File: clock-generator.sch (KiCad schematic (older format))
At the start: 7 parts

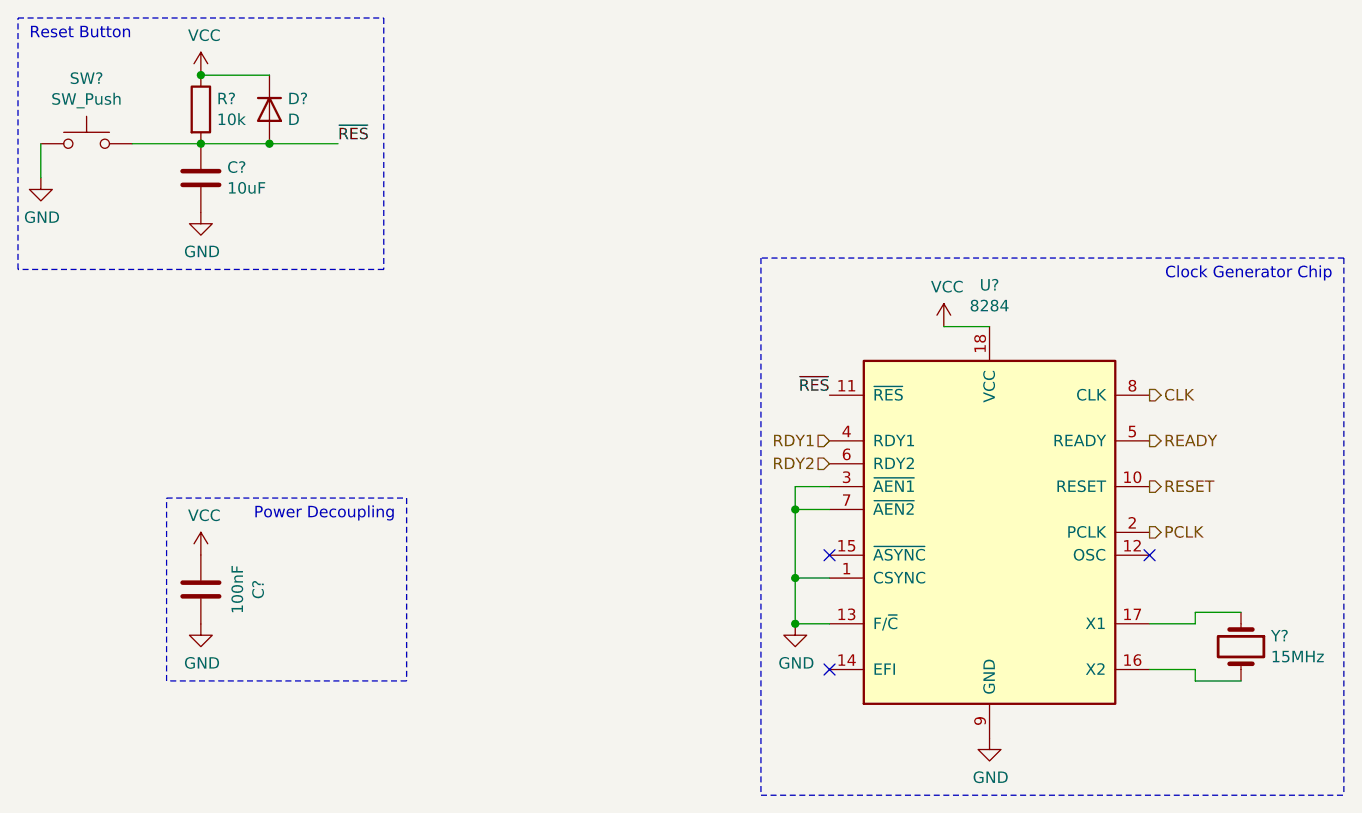
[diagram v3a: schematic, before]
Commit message: General edits; removed floating inputs
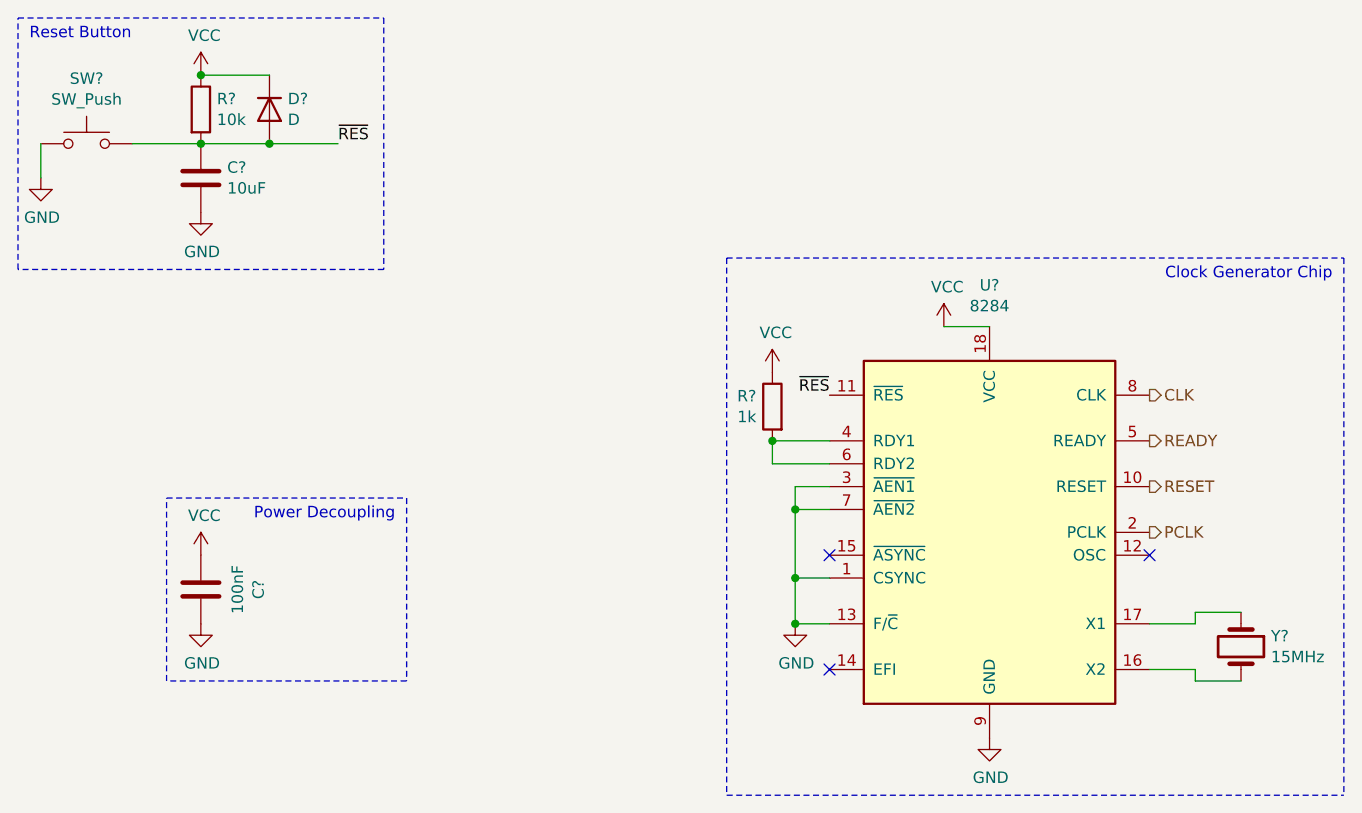
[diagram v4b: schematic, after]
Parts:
- added R?: 1k, symbol Device:R
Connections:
- net RDY2 is gone; now on an unnamed net: U?.6 (RDY2)
- net VCC: now also R?.1
- net RDY1: no longer names the net of U?.4 (RDY1)
- net RDY1: now also R?.2
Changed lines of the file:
@@
 $Descr A4 11693 8268
 encoding utf-8
-Sheet 4 15
+Sheet 3 15
 Title "clock-generator"
 Date ""
@@
 Text HLabel 6400 3200 2    50   Output ~ 0
 READY
-Text HLabel 5000 3200 0    50   Input ~ 0
-RDY1
-Text HLabel 5000 3300 0    50   Input ~ 0
-RDY2
 NoConn ~ 5000 3700
 Wire Wire Line
@@
 $EndComp
 Wire Notes Line
-	7250 2400 4700 2400
-Wire Notes Line
-	4700 2400 4700 4750
-Wire Notes Line
-	4700 4750 7250 4750
-Wire Notes Line
 	7250 2400 7250 4750
 Text Notes 7200 2500 2    50   ~ 0
@@
 Text Notes 1500 1450 0    50   ~ 0
 Reset Button
+Wire Wire Line
+	5000 3300 4750 3300
+Wire Wire Line
+	5000 3200 4750 3200
+Wire Wire Line
+	4750 3300 4750 3200
+$Comp
+L Device:R R?
+U 1 1 61F71673
+P 4750 3050
+F 0 "R?" H 4820 3096 50  0000 L CNN
+F 1 "1k" H 4820 3005 50  0000 L CNN
+F 2 "" V 4680 3050 50  0001 C CNN
+F 3 "~" H 4750 3050 50  0001 C CNN
+	1    4750 3050
+	-1   0    0    -1
+$EndComp
+$Comp
+L power:VCC #PWR?
+U 1 1 61F75C77
+P 4750 2900
+F 0 "#PWR?" H 4750 2750 50  0001 C CNN
+F 1 "VCC" H 4765 3073 50  0000 C CNN
+F 2 "" H 4750 2900 50  0001 C CNN
+F 3 "" H 4750 2900 50  0001 C CNN
+	1    4750 2900
+	1    0    0    -1
+$EndComp
+Connection ~ 4750 3200
+Wire Notes Line
+	4550 2400 4550 4750
+Wire Notes Line
+	4550 2400 7250 2400
+Wire Notes Line
+	4550 4750 7250 4750
 $EndSCHEMATC

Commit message: Assign footprints for most symbols
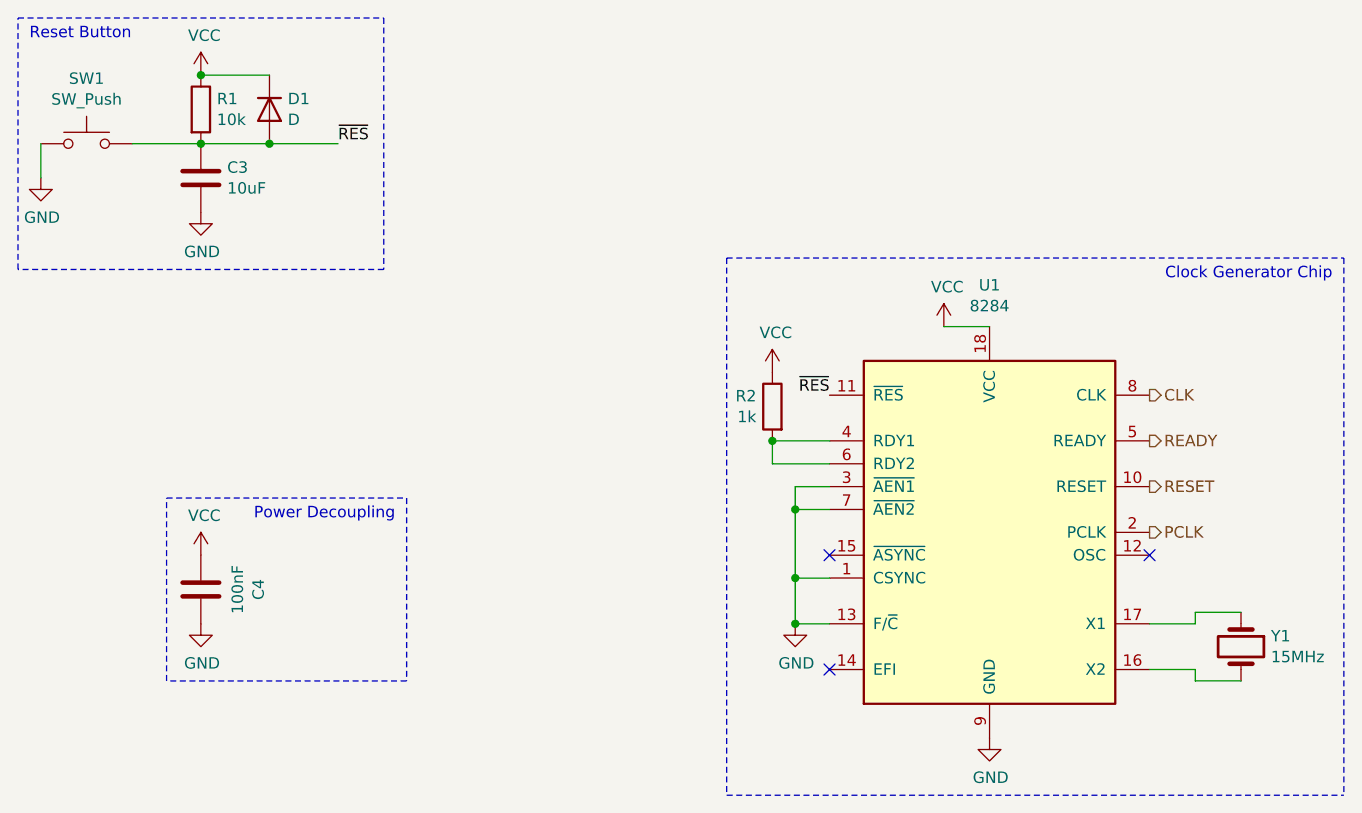
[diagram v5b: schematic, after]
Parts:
- C4: renamed from C?; footprint (none) -> Capacitor_THT:C_Rect_L4.0mm_W2.5mm_P2.50mm
- D1: renamed from D?; footprint (none) -> Diode_THT:D_DO-35_SOD27_P7.62mm_Horizontal
- R1, R2: renamed from R?; footprint (none) -> Resistor_THT:R_Axial_DIN0207_L6.3mm_D2.5mm_P10.16mm_Horizontal
- SW1: renamed from SW?; footprint (none) -> Button_Switch_Keyboard:SW_Cherry_MX_1.00u_PCB
- gave numbers to parts that had none: 3
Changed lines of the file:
@@
 $EndDescr
 $Comp
-L Timer:8284 U?
+L Timer:8284 U1
 U 1 1 61931D8C
 P 5700 3600
-F 0 "U?" H 5700 4681 50  0000 C CNN
+F 0 "U1" H 5700 4681 50  0000 C CNN
 F 1 "8284" H 5700 4590 50  0000 C CNN
 F 2 "Package_DIP:DIP-18_W7.62mm" H 5700 3600 50  0001 C CIN
@@
 $EndComp
 $Comp
-L Device:C C?
+L Device:C C4
 U 1 1 61933DA5
 P 2250 3850
-F 0 "C?" V 2502 3850 50  0000 C CNN
+F 0 "C4" V 2502 3850 50  0000 C CNN
 F 1 "100nF" V 2411 3850 50  0000 C CNN
-F 2 "" H 2288 3700 50  0001 C CNN
+F 2 "Capacitor_THT:C_Rect_L4.0mm_W2.5mm_P2.50mm" H 2288 3700 50  0001 C CNN
 F 3 "~" H 2250 3850 50  0001 C CNN
 	1    2250 3850
@@
 Connection ~ 4850 4000
 $Comp
-L Device:Crystal Y?
+L Device:Crystal Y1
 U 1 1 6193AF6D
 P 6800 4100
-F 0 "Y?" V 6754 4231 50  0000 L CNN
+F 0 "Y1" V 6754 4231 50  0000 L CNN
 F 1 "15MHz" V 6845 4231 50  0000 L CNN
 F 2 "" H 6800 4100 50  0001 C CNN
@@
 ~RES
 $Comp
-L Switch:SW_Push SW?
+L Switch:SW_Push SW1
 U 1 1 6193E6E5
 P 1750 1900
-F 0 "SW?" H 1750 2185 50  0000 C CNN
+F 0 "SW1" H 1750 2185 50  0000 C CNN
 F 1 "SW_Push" H 1750 2094 50  0000 C CNN
-F 2 "" H 1750 2100 50  0001 C CNN
+F 2 "Button_Switch_Keyboard:SW_Cherry_MX_1.00u_PCB" H 1750 2100 50  0001 C CNN
 F 3 "~" H 1750 2100 50  0001 C CNN
 	1    1750 1900
@@
 $EndComp
 $Comp
-L Device:R R?
+L Device:R R1
 U 1 1 6193FE29
 P 2250 1750
-F 0 "R?" H 2320 1796 50  0000 L CNN
+F 0 "R1" H 2320 1796 50  0000 L CNN
 F 1 "10k" H 2320 1705 50  0000 L CNN
-F 2 "" V 2180 1750 50  0001 C CNN
+F 2 "Resistor_THT:R_Axial_DIN0207_L6.3mm_D2.5mm_P10.16mm_Horizontal" V 2180 1750 50  0001 C CNN
 F 3 "~" H 2250 1750 50  0001 C CNN
 	1    2250 1750
@@
 $EndComp
 $Comp
-L Device:C C?
+L Device:C C3
 U 1 1 619403B8
 P 2250 2050
-F 0 "C?" H 2365 2096 50  0000 L CNN
+F 0 "C3" H 2365 2096 50  0000 L CNN
 F 1 "10uF" H 2365 2005 50  0000 L CNN
 F 2 "" H 2288 1900 50  0001 C CNN
@@
 ~RES
 $Comp
-L Device:D D?
+L Device:D D1
 U 1 1 6194EDFA
 P 2550 1750
-F 0 "D?" V 2504 1830 50  0000 L CNN
+F 0 "D1" V 2504 1830 50  0000 L CNN
 F 1 "D" V 2595 1830 50  0000 L CNN
-F 2 "" H 2550 1750 50  0001 C CNN
+F 2 "Diode_THT:D_DO-35_SOD27_P7.62mm_Horizontal" H 2550 1750 50  0001 C CNN
 F 3 "~" H 2550 1750 50  0001 C CNN
 	1    2550 1750
@@
 	4850 3500 4850 3800
 $Comp
-L power:VCC #PWR?
+L power:VCC #PWR0106
 U 1 1 61C7475F
 P 2250 3700
-F 0 "#PWR?" H 2250 3550 50  0001 C CNN
+F 0 "#PWR0106" H 2250 3550 50  0001 C CNN
 F 1 "VCC" H 2265 3873 50  0000 C CNN
 F 2 "" H 2250 3700 50  0001 C CNN
@@
 $EndComp
 $Comp
-L power:VCC #PWR?
+L power:VCC #PWR0107
 U 1 1 61C74E11
 P 5500 2700
-F 0 "#PWR?" H 5500 2550 50  0001 C CNN
+F 0 "#PWR0107" H 5500 2550 50  0001 C CNN
 F 1 "VCC" H 5515 2873 50  0000 C CNN
 F 2 "" H 5500 2700 50  0001 C CNN
@@
 	4750 3300 4750 3200
 $Comp
-L Device:R R?
+L Device:R R2
 U 1 1 61F71673
 P 4750 3050
-F 0 "R?" H 4820 3096 50  0000 L CNN
+F 0 "R2" H 4820 3096 50  0000 L CNN
 F 1 "1k" H 4820 3005 50  0000 L CNN
-F 2 "" V 4680 3050 50  0001 C CNN
+F 2 "Resistor_THT:R_Axial_DIN0207_L6.3mm_D2.5mm_P10.16mm_Horizontal" V 4680 3050 50  0001 C CNN
 F 3 "~" H 4750 3050 50  0001 C CNN
 	1    4750 3050
@@
 $EndComp
 $Comp
-L power:VCC #PWR?
+L power:VCC #PWR0108
 U 1 1 61F75C77
 P 4750 2900
-F 0 "#PWR?" H 4750 2750 50  0001 C CNN
+F 0 "#PWR0108" H 4750 2750 50  0001 C CNN
 F 1 "VCC" H 4765 3073 50  0000 C CNN
 F 2 "" H 4750 2900 50  0001 C CNN

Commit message: Assigned footprints
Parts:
- C3: footprint (none) -> Capacitor_THT:C_Rect_L4.6mm_W3.8mm_P2.50mm_MKS02_FKP02
- Y1: footprint (none) -> Crystal:Crystal_HC49-4H_Vertical
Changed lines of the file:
@@
 F 0 "Y1" V 6754 4231 50  0000 L CNN
 F 1 "15MHz" V 6845 4231 50  0000 L CNN
-F 2 "" H 6800 4100 50  0001 C CNN
+F 2 "Crystal:Crystal_HC49-4H_Vertical" H 6800 4100 50  0001 C CNN
 F 3 "~" H 6800 4100 50  0001 C CNN
 	1    6800 4100
@@
 F 0 "C3" H 2365 2096 50  0000 L CNN
 F 1 "10uF" H 2365 2005 50  0000 L CNN
-F 2 "" H 2288 1900 50  0001 C CNN
+F 2 "Capacitor_THT:C_Rect_L4.6mm_W3.8mm_P2.50mm_MKS02_FKP02" H 2288 1900 50  0001 C CNN
 F 3 "~" H 2250 2050 50  0001 C CNN
 	1    2250 2050

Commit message: begin pcb layout
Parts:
- SW1: value SW_Push -> RESET
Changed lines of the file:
@@
 P 1750 1900
 F 0 "SW1" H 1750 2185 50  0000 C CNN
-F 1 "SW_Push" H 1750 2094 50  0000 C CNN
+F 1 "RESET" H 1750 2094 50  0000 C CNN
 F 2 "Button_Switch_Keyboard:SW_Cherry_MX_1.00u_PCB" H 1750 2100 50  0001 C CNN
 F 3 "~" H 1750 2100 50  0001 C CNN
